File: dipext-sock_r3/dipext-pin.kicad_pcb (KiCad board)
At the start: 2 copper layers, 63.8 x 68.3 mm, 8 parts, among them J1 ZIF, J2 IDC40, J3 Conn_02x20_Odd_Even, J4 Conn_02x20_Odd_Even, J5 01x20, J6 01x20, J7 01x20, J8 01x20

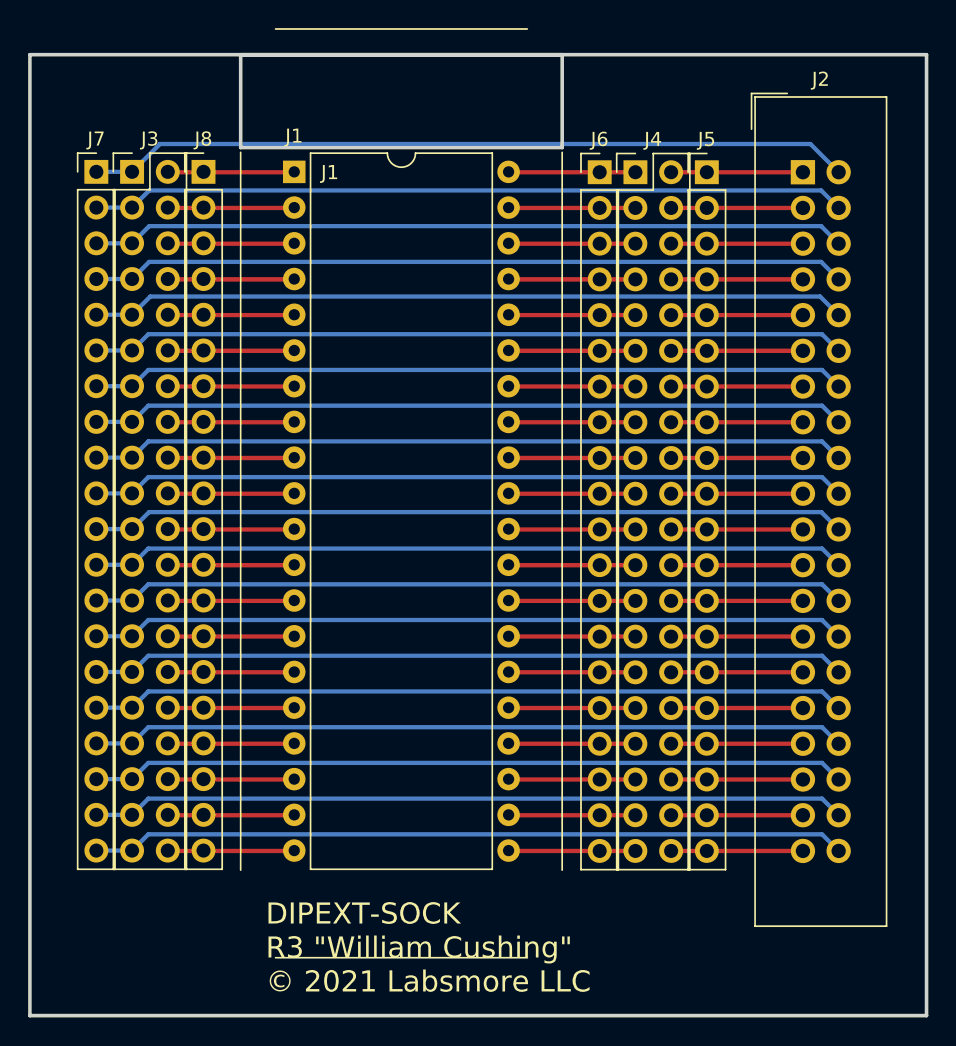
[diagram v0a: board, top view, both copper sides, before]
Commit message: Fixes to cut  lines.
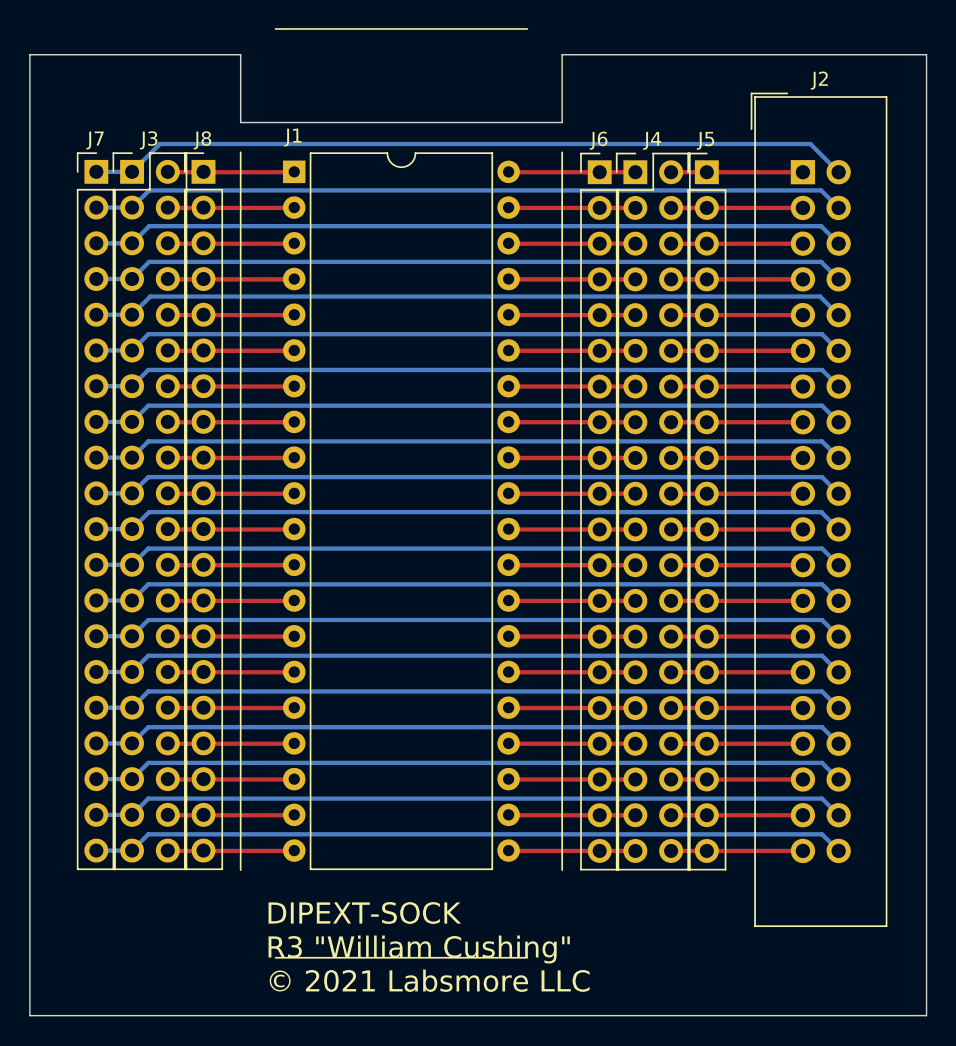
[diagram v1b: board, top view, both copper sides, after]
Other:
- outline, holes or cut-outs redrawn
- board text removed: "J1"
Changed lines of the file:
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@@
     )
   )
-  (gr_rect (start 53.086 38.1) (end 75.946 44.704) (layer "Edge.Cuts") (width 0.254) (fill none))
-  (gr_rect (start 101.854 38.1) (end 38.1 106.426) (layer "Edge.Cuts") (width 0.254) (fill none))
+  (gr_line (start 75.946 38.1) (end 75.946 42.926) (layer "Edge.Cuts") (width 0.1))
+  (gr_line (start 101.854 106.426) (end 101.854 38.1) (layer "Edge.Cuts") (width 0.1))
+  (gr_line (start 38.1 38.1) (end 38.1 106.426) (layer "Edge.Cuts") (width 0.1))
+  (gr_line (start 53.086 42.926) (end 53.086 38.1) (layer "Edge.Cuts") (width 0.1))
+  (gr_line (start 75.946 38.1) (end 101.854 38.1) (layer "Edge.Cuts") (width 0.1))
+  (gr_line (start 53.086 42.926) (end 75.946 42.926) (layer "Edge.Cuts") (width 0.1))
+  (gr_line (start 101.854 106.426) (end 38.1 106.426) (layer "Edge.Cuts") (width 0.1))
+  (gr_line (start 38.1 38.1) (end 53.086 38.1) (layer "Edge.Cuts") (width 0.1))
   (gr_text "DIPEXT-SOCK\nR3 {dblquote}William Cushing{dblquote}\n© 2021 Labsmore LLC" (at 54.864 101.6) (layer "F.SilkS")
     (effects (font (size 1.5 1.5) (thickness 0.3)) (justify left))
   )
-  (gr_text "J1" (at 59.436 46.482) (layer "F.SilkS")
-    (effects (font (size 1 1) (thickness 0.15)))
-  )
   (segment (start 42.824399 46.431201) (end 45.364399 46.431201) (width 0.3048) (layer "B.Cu") (net 1))
